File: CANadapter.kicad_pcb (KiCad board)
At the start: 2 copper layers, 94 x 22.9 mm, 28 parts, among them P1 CONN_02X06, P2 CONN_01X06, P3 CONN_01X04, P4 CONN_01X06, U1 MCP2515, U2 TLP2361, U3 TLP2361, U4 MCP2551-I/SN, U5 LM7805CT, U6 NKE0305SC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

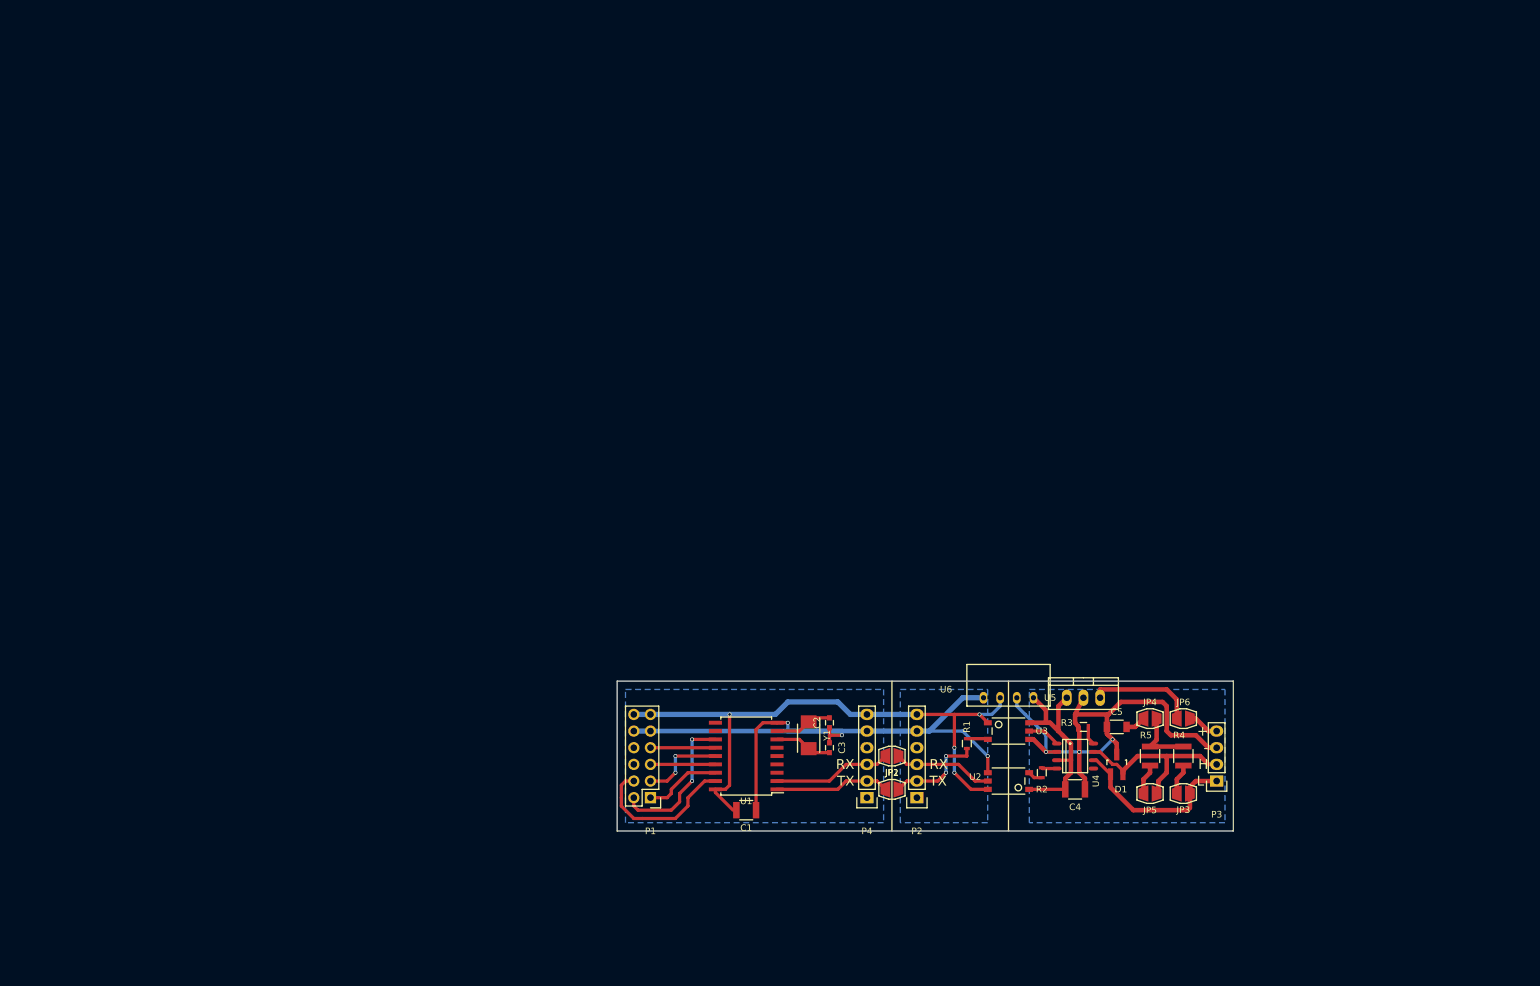
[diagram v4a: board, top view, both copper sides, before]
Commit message: finished routing, improved silk
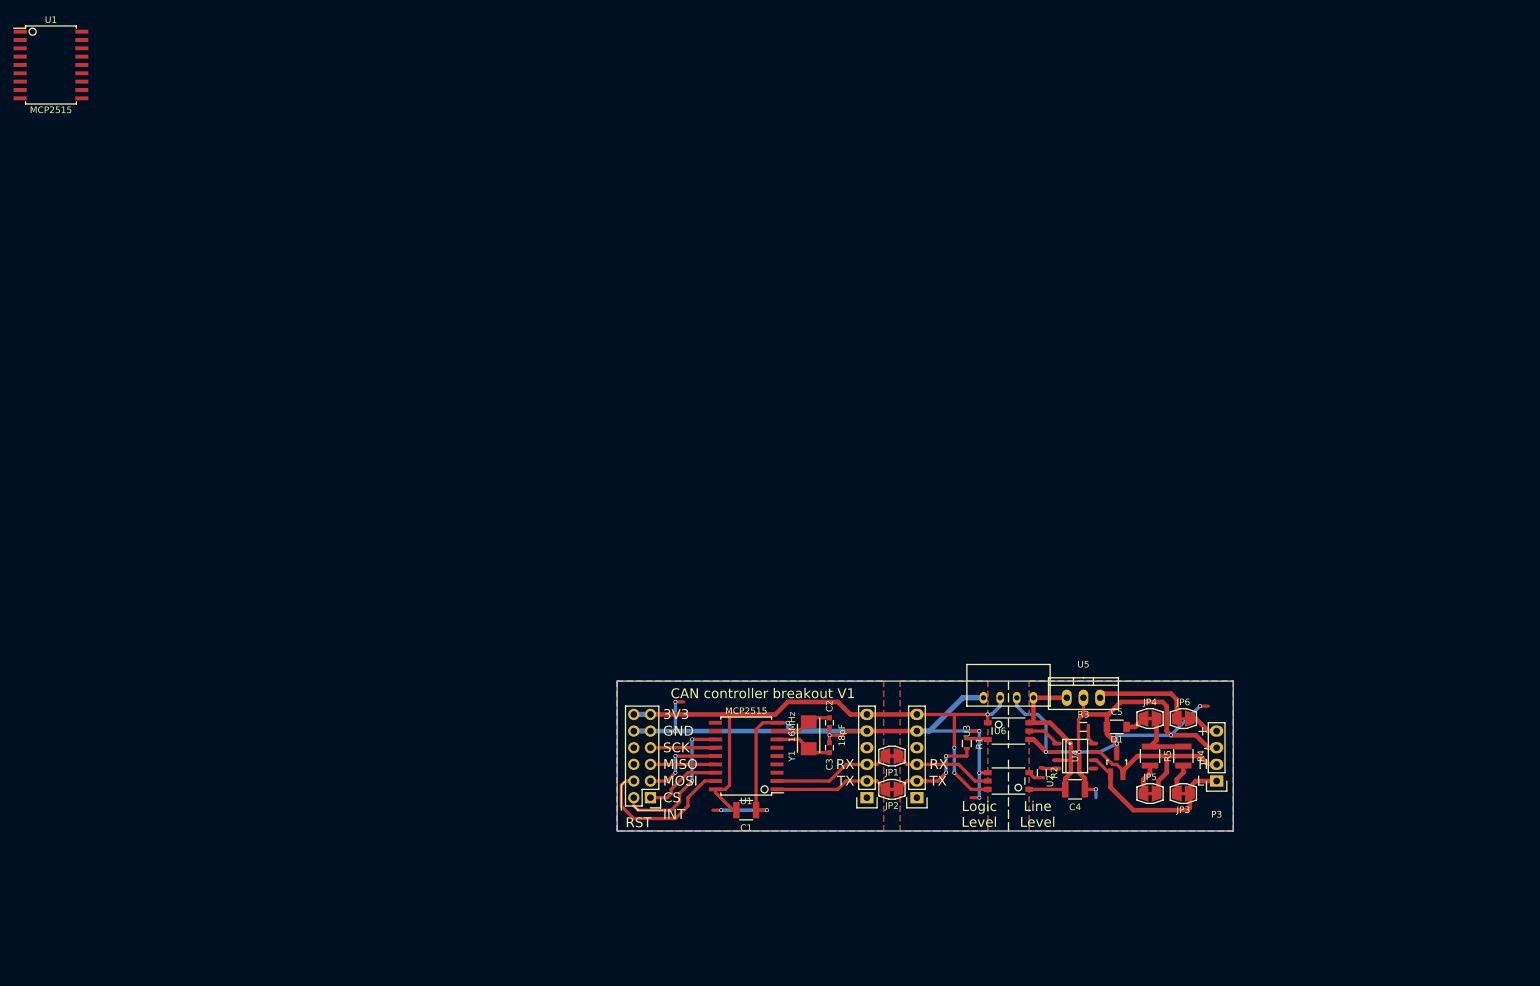
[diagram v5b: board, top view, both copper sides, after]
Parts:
- removed the U1 at (106.0, 105.4)
- added U1: MCP2515, LocalLib:SOIC-18_7.5x11.6mm_Pitch1.27mm, F.Cu at (106.0, 105.4)
- added U1: MCP2515, LocalLib:SOIC-18_7.5x11.6mm_Pitch1.27mm, F.Cu at (0.00, 0.00)
- JP1, JP2: footprint LocalLib:JumperSingleJumbo -> LocalLib:JumperSingleClosed
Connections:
- P1 pad 6: (no net) -> Net-(P1-Pad6)
- P1 pad 8: (no net) -> Net-(P1-Pad8)
- P2 pad 1: (no net) -> Net-(P2-Pad1)
- P2 pad 4: (no net) -> Net-(P2-Pad4)
- P4 pad 1: (no net) -> Net-(P4-Pad1)
- P4 pad 4: (no net) -> Net-(P4-Pad4)
- U4 pad 5: (no net) -> Net-(U4-Pad5)
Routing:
- net GND: track 94.1 -> 116.7 mm, vias 3 -> 7
- net GNDREF: track 75.3 -> 95.1 mm, vias 3 -> 6
- net (no net): track 0.00 -> 5.71 mm, vias 0 -> 2
- net +5V: track 32.9 -> 31.6 mm
- net Net-(JP6-Pad2): track 16.5 -> 15.2 mm
- net +3V3: track 93.6 -> 93.1 mm, vias 4 -> 3
- added copper zone on F.Cu, net GND
- added copper zone on F.Cu, net GNDREF
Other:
- board text added: "BrettRD 2016"
- board text added: "CAN controller breakout V1"
- board text added: "CAN interface V1"
- board text added: "Line Level"
- board text added: "Logic Level"

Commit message: improved silk
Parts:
- removed the U1 at (0.00, 0.00)
- JP6: value Line Power -> Power
- U4: value MCP2551-I/SN -> MCP2551
- U5: value LM7805CT -> 7805
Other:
- board text added: "CAN adapter V1"

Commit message: ready for beta round
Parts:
- JP3, JP4, JP5, JP6: footprint LocalLib:JumperSingleJumbo -> LocalLib:JumperSingle
- moved C1 105.2 mm to (34.9, 36.2)
- moved C2 105.2 mm to (47.6, 22.9)
- moved C3 105.2 mm to (47.6, 26.7)
- moved C4 105.2 mm to (85.1, 33.0)
- moved C5 105.2 mm to (91.4, 23.5)
- moved D1 105.2 mm to (91.4, 29.2)
- moved JP1 105.2 mm to (57.1, 27.9)
- moved JP2 105.2 mm to (57.1, 33.0)
- moved JP3 105.2 mm to (101.6, 33.7)
- moved JP4 105.2 mm to (96.5, 22.2)
- moved JP5 105.2 mm to (96.5, 33.7)
- moved JP6 105.2 mm to (101.6, 22.2)
- moved P1 105.2 mm to (20.3, 34.3)
- moved P2 105.2 mm to (61.0, 34.3)
- moved P3 105.2 mm to (106.7, 31.8)
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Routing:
- net (no net): track 5.71 -> 0.00 mm, vias 2 -> 0
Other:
- board text added: "5V"
- board text added: "CAN controller"
- board text added: "CAN interface"
- board text removed: "CAN controller breakout V1"
- board text removed: "CAN interface V1"
- board text removed: "Controller"
- board text removed: "Interface"
- board text removed: "Isolation"
